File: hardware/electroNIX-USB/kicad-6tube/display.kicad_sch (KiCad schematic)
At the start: 87 parts, among them Q10 MMBTA42, Q11 MMBTA92, Q12 MMBTA42, Q13 MMBTA92, Q14 MMBTA42, Q15 MMBTA92, Q16 MMBTA42, Q17 MMBTA42, Q18 MMBTA42, Q19 MMBTA42, Q20 MMBTA42, Q21 MMBTA42, Q22 MMBTA42, Q23 MMBTA42, Q24 MMBTA42, Q25 MMBTA42, Q26 MMBTA42, Q27 MMBTA42, Q4 MMBTA42, Q5 MMBTA92, Q6 MMBTA42, Q7 MMBTA92, Q8 MMBTA42, Q9 MMBTA92

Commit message: electroNIX-USB: drop all switches, regroup board placement by circuit
- No RESET/BOOT/SET: the firmware reads no button, and the CH340C
  DTR/RTS auto-reset handles flashing. SET's pull-up and cap are gone.
- Boost converter is a compact loop (input caps -> L1 -> FET tab) feeding
  the multiplier columns in chain order.
- ESP32: 3V3 decoupling at pin 2, EN RC at pin 3, HV feedback divider and
  clamp at IO35; auto-reset between the CH340C and the module's UART pins.
- Front band spread out: output cap + KBIAS left, cathode row, one anode
  cluster under each tube.
- 6-tube board placed too (150 x 66 mm). Both boards unrouted.

Co-Authored-By: Claude Opus 5.5 <noreply@anthropic.com>
Claude-Session: https://claude.ai/code/session_01AFMfevKEKDGbci8uJGhf4W
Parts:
- removed C22: 2u2 50V, Capacitor_SMD:C_1206_3216Metric, symbol Device:C
- removed R54: 100k, Resistor_SMD:R_0805_2012Metric, symbol Device:R
- added C21: 2u2 50V, Capacitor_SMD:C_1206_3216Metric, symbol Device:C
- added R12: 15k, Resistor_SMD:R_0805_2012Metric, symbol Device:R
- R13, R17, R21, R25, R29, R33: value 15k -> 430k; footprint Resistor_SMD:R_0805_2012Metric -> Resistor_SMD:R_1206_3216Metric
- R14, R18, R22, R26, R30, R34, R53: value 430k -> 100k; footprint Resistor_SMD:R_1206_3216Metric -> Resistor_SMD:R_0805_2012Metric
- R15, R19, R23, R27, R31, R35: value 100k -> 3k9
- R16, R20, R24, R28, R32: value 3k9 -> 15k
- R36: value 3k9 -> 6k8
- R46: value 6k8 -> 47k
- R47, R50: value 47k -> 150k; footprint Resistor_SMD:R_0805_2012Metric -> Resistor_SMD:R_1206_3216Metric
- R49: value 150k -> 47k; footprint Resistor_SMD:R_1206_3216Metric -> Resistor_SMD:R_0805_2012Metric
- R52: value 150k -> 430k
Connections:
- net +170V: now also R14.1, R18.1, R22.1, R26.1, R30.1, R34.1, R47.1, R50.1; no longer R15.1, R19.1, R23.1, R27.1, R31.1, R35.1, R49.1, R53.1
- net A_1: now also R15.2; no longer R16.2
- net A_2: now also R19.2; no longer R20.2
- net A_3: now also R23.2; no longer R24.2
- net A_4: now also R27.2; no longer R28.2
- net A_5: now also R31.2; no longer R32.2
- net A_6: now also R35.2; no longer R36.2
- net C_0: now also R36.1; no longer R37.1
- net C_1: now also R37.1; no longer R38.1
- net C_2: now also R38.1; no longer R39.1
- net C_3: now also R39.1; no longer R40.1
- net C_4: now also R40.1; no longer R41.1
- net C_5: now also R41.1; no longer R42.1
- net C_6: now also R42.1; no longer R43.1
- net C_7: now also R43.1; no longer R44.1
- net C_8: now also R44.1; no longer R45.1
- net C_9: now also R45.1; no longer R46.1
- net GND: now also R53.2, C21.2
- net KBIAS: now also R52.2, R53.1, C21.1; no longer R53.2
- net SEC_0: now also R46.1; no longer R47.1
- net SEC_1: now also R49.1; no longer R50.1
- net W_1: now also R12.1; no longer R13.1
- net W_2: now also R16.1; no longer R17.1
- net W_3: now also R20.1; no longer R21.1
- net W_4: now also R24.1; no longer R25.1
- net W_5: now also R28.1; no longer R29.1
- net W_6: now also R32.1; no longer R33.1
- net at Q6.1 (B): now also R16.2; no longer R17.2
- net at Q6.3 (C): now also R17.2; no longer R18.2
- net at Q7.3 (C): now also R19.1; no longer R20.1
- net at Q9.3 (C): now also R23.1; no longer R24.1
- net at R51.2: now also NE4.2; no longer NE3.2
- net at Q11.3 (C): now also R27.1; no longer R28.1
- net at Q5.3 (C): now also R15.1; no longer R16.1
- net at Q20.1 (B): now also R40.2; no longer R41.2
- net at R34.2: now also Q15.1 (B), R33.1; no longer Q14.3 (C)
- net at Q14.1 (B): now also R32.2; no longer R33.2
- net at Q25.1 (B): now also R45.2; no longer R46.2
- net at R47.2: now also NE1.2; no longer Q26.1 (B)
- net at Q15.3 (C): now also R35.1; no longer R36.1
- net at Q12.1 (B): now also R28.2; no longer R29.2
- net at Q19.1 (B): now also R39.2; no longer R40.2
- net at Q18.1 (B): now also R38.2; no longer R39.2
- net at Q24.1 (B): now also R44.2; no longer R45.2
- net at Q17.1 (B): now also R37.2; no longer R38.2
- net at Q13.3 (C): now also R31.1; no longer R32.1
- net at Q16.1 (B): now also R36.2; no longer R37.2
- net at R50.2: now also NE3.2; no longer Q27.1 (B)
- net at Q4.1 (B): now also R12.2; no longer R13.2
- net at R14.2: now also Q5.1 (B), R13.1; no longer Q4.3 (C)
- net at Q8.1 (B): now also R20.2; no longer R21.2
- net at Q8.3 (C): now also R21.2; no longer R22.2
- net at Q10.1 (B): now also R24.2; no longer R25.2
- net at R26.2: now also Q11.1 (B), R25.1; no longer Q10.3 (C)
- net at R30.2: now also Q13.1 (B), R29.1; no longer Q12.3 (C)
- net at R48.2: now also NE2.2; no longer NE1.2
- net at R49.2: now also Q27.1 (B); no longer NE2.2
- net at Q23.1 (B): now also R43.2; no longer R44.2
- net at Q21.1 (B): now also R41.2; no longer R42.2
- net at Q22.1 (B): now also R42.2; no longer R43.2
- new net: Q7.1 (B), R17.1, R18.2
- new net: Q14.3 (C), R33.2
- new net: Q12.3 (C), R29.2
- new net: Q4.3 (C), R13.2
- new net: Q10.3 (C), R25.2
- new net: Q9.1 (B), R21.1, R22.2
- new net: Q26.1 (B), R46.2
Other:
- moved on the sheet: R13, R14, R15, R16, R17, R18, R19, R20, R21, R22, R23, R24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

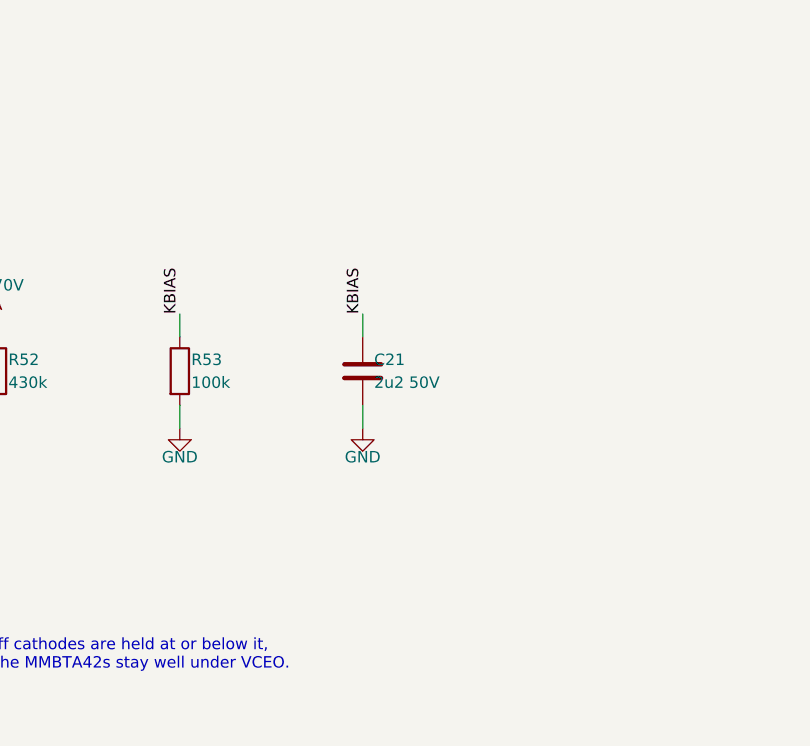
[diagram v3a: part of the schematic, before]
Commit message: electroNIX-USB: restore PCB-036 KBIAS capacitor string (4 x 470n in series)
C41-C44 on PCB-036 are in series (118 nF, 200 V string) across R46, not
in parallel. Replace the single 2.2 uF/50 V cap with the original series
string and place it beside the 430k/100k divider.

Co-Authored-By: Claude Opus 5.5 <noreply@anthropic.com>
Claude-Session: https://claude.ai/code/session_01AFMfevKEKDGbci8uJGhf4W
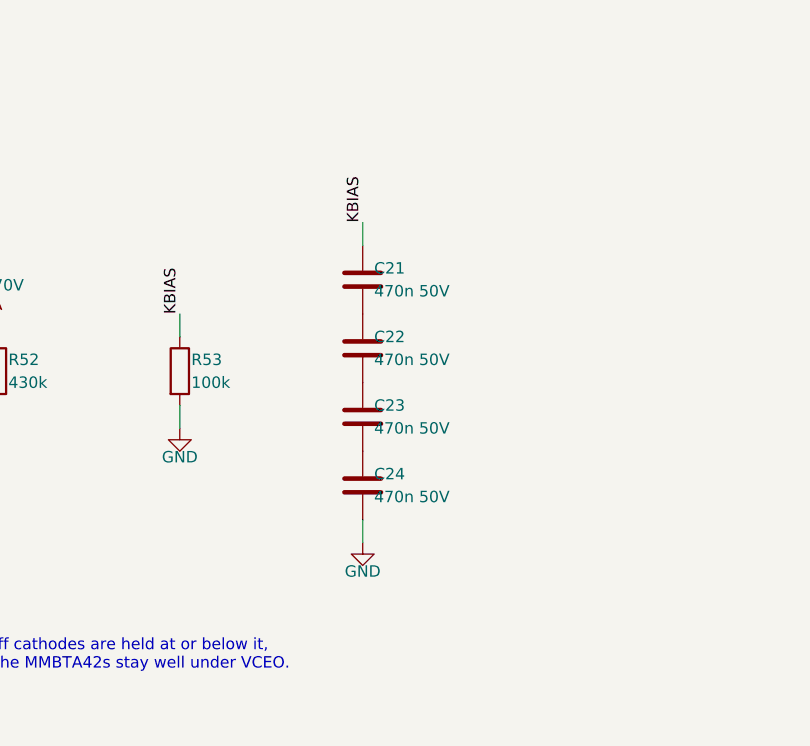
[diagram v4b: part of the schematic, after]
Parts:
- added C22, C23, C24: 470n 50V, Capacitor_SMD:C_0805_2012Metric, symbol Device:C
- C21: value 2u2 50V -> 470n 50V; footprint Capacitor_SMD:C_1206_3216Metric -> Capacitor_SMD:C_0805_2012Metric
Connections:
- net GND: now also C24.2; no longer C21.2
- new net: C21.2, C22.1
- new net: C22.2, C23.1
- new net: C23.2, C24.1
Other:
- moved on the sheet: C21
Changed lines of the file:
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@@
   (wire
     (pts
-      (xy 490.22 246.38)
-      (xy 490.22 243.84))
+      (xy 490.22 236.22)
+      (xy 490.22 233.68))
     (stroke
       (width 0)
@@
   (wire
     (pts
-      (xy 490.22 254)
-      (xy 490.22 256.54))
+      (xy 490.22 266.7)
+      (xy 490.22 269.24))
     (stroke
       (width 0)
@@
 )
   (label "KBIAS"
-    (at 490.22 243.84 90)
+    (at 490.22 233.68 90)
     (fields_autoplaced)
     (effects
@@
           (unit 1)))))
   (symbol
+    (lib_id "Device:C")
+    (at 490.22 240.03 0)
+    (unit 1)
+    (in_bom yes)
+    (on_board yes)
+    (dnp no)
+    (property "Reference" "C21"
+      (at 491.49 238.76 0)
+      (effects
+        (font
+          (size 1.27 1.27))
+        (justify left)))
+    (property "Value" "470n 50V"
+      (at 491.49 241.3 0)
+      (effects
+        (font
+          (size 1.27 1.27))
+        (justify left)))
+    (property "Footprint" "Capacitor_SMD:C_0805_2012Metric"
+      (at 490.22 240.03 0)
+      (effects
+        (font
+          (size 1.27 1.27))
+        (justify left) hide))
+    (property "Datasheet" "~"
+      (at 490.22 240.03 0)
+      (effects
+        (font
+          (size 1.27 1.27))
+        (justify left) hide))
+    (pin "1"
+)
+    (pin "2"
+)
+    (instances
+      (project "electroNIX-USB"
+        (path "/af167dc7-e2c9-570c-bdf4-28156a519677/e1c1bd65-1db2-544e-8cf9-3d73564eba6a"
+          (reference "C21")
+          (unit 1)))))
+  (symbol
+    (lib_id "Device:C")
+    (at 490.22 247.65 0)
+    (unit 1)
+    (in_bom yes)
+    (on_board yes)
+    (dnp no)
+    (property "Reference" "C22"
+      (at 491.49 246.38 0)
+      (effects
+        (font
+          (size 1.27 1.27))
+        (justify left)))
+    (property "Value" "470n 50V"
+      (at 491.49 248.92 0)
+      (effects
+        (font
+          (size 1.27 1.27))
+        (justify left)))
+    (property "Footprint" "Capacitor_SMD:C_0805_2012Metric"
+      (at 490.22 247.65 0)
+      (effects
+        (font
+          (size 1.27 1.27))
+        (justify left) hide))
+    (property "Datasheet" "~"
+      (at 490.22 247.65 0)
+      (effects
+        (font
+          (size 1.27 1.27))
+        (justify left) hide))
+    (pin "1"
+)
+    (pin "2"
+)
+    (instances
+      (project "electroNIX-USB"
+        (path "/af167dc7-e2c9-570c-bdf4-28156a519677/e1c1bd65-1db2-544e-8cf9-3d73564eba6a"
+          (reference "C22")
+          (unit 1)))))
+  (symbol
+    (lib_id "Device:C")
+    (at 490.22 255.27 0)
+    (unit 1)
+    (in_bom yes)
+    (on_board yes)
+    (dnp no)
+    (property "Reference" "C23"
+      (at 491.49 254 0)
+      (effects
+        (font
+          (size 1.27 1.27))
+        (justify left)))
+    (property "Value" "470n 50V"
+      (at 491.49 256.54 0)
+      (effects
+        (font
+          (size 1.27 1.27))
+        (justify left)))
+    (property "Footprint" "Capacitor_SMD:C_0805_2012Metric"
+      (at 490.22 255.27 0)
+      (effects
+        (font
+          (size 1.27 1.27))
+        (justify left) hide))
+    (property "Datasheet" "~"
+      (at 490.22 255.27 0)
+      (effects
+        (font
+          (size 1.27 1.27))
+        (justify left) hide))
+    (pin "1"
+)
+    (pin "2"
+)
+    (instances
+      (project "electroNIX-USB"
+        (path "/af167dc7-e2c9-570c-bdf4-28156a519677/e1c1bd65-1db2-544e-8cf9-3d73564eba6a"
+          (reference "C23")
+          (unit 1)))))
+  (symbol
     (lib_id "power:GND")
-    (at 490.22 256.54 0)
+    (at 490.22 269.24 0)
     (unit 1)
     (in_bom yes)
     (on_board yes)
     (dnp no)
-    (property "Reference" "#PWR5122"
-      (at 490.22 256.54 0)
+    (property "Reference" "#PWR5125"
+      (at 490.22 269.24 0)
       (effects
         (font
           (size 1.27 1.27)) hide))
     (property "Value" "GND"
-      (at 490.22 259.74 0)
+      (at 490.22 272.44 0)
       (effects
         (font
           (size 1.27 1.27))))
     (property "Footprint" ""
-      (at 490.22 256.54 0)
+      (at 490.22 269.24 0)
       (effects
         (font
           (size 1.27 1.27)) hide))
     (property "Datasheet" ""
-      (at 490.22 256.54 0)
+      (at 490.22 269.24 0)
       (effects
         (font
@@
       (project "electroNIX-USB"
         (path "/af167dc7-e2c9-570c-bdf4-28156a519677/e1c1bd65-1db2-544e-8cf9-3d73564eba6a"
-          (reference "#PWR5122")
+          (reference "#PWR5125")
           (unit 1)))))
   (symbol
     (lib_id "Device:C")
-    (at 490.22 250.19 0)
+    (at 490.22 262.89 0)
     (unit 1)
     (in_bom yes)
     (on_board yes)
     (dnp no)
-    (property "Reference" "C21"
-      (at 491.49 248.92 0)
+    (property "Reference" "C24"
+      (at 491.49 261.62 0)
       (effects
         (font
           (size 1.27 1.27))
         (justify left)))
-    (property "Value" "2u2 50V"
-      (at 491.49 251.46 0)
+    (property "Value" "470n 50V"
+      (at 491.49 264.16 0)
       (effects
         (font
           (size 1.27 1.27))
         (justify left)))
-    (property "Footprint" "Capacitor_SMD:C_1206_3216Metric"
-      (at 490.22 250.19 0)
+    (property "Footprint" "Capacitor_SMD:C_0805_2012Metric"
+      (at 490.22 262.89 0)
       (effects
         (font
@@
         (justify left) hide))
     (property "Datasheet" "~"
-      (at 490.22 250.19 0)
+      (at 490.22 262.89 0)
       (effects
         (font
@@
       (project "electroNIX-USB"
         (path "/af167dc7-e2c9-570c-bdf4-28156a519677/e1c1bd65-1db2-544e-8cf9-3d73564eba6a"
-          (reference "C21")
+          (reference "C24")
           (unit 1))))))
